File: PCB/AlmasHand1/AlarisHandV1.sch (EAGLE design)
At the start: 13 parts, among them M1 22-23-2021, M2 22-23-2021, M3 22-23-2021, M4 22-23-2021, M5 22-23-2021, M6 22-23-2021

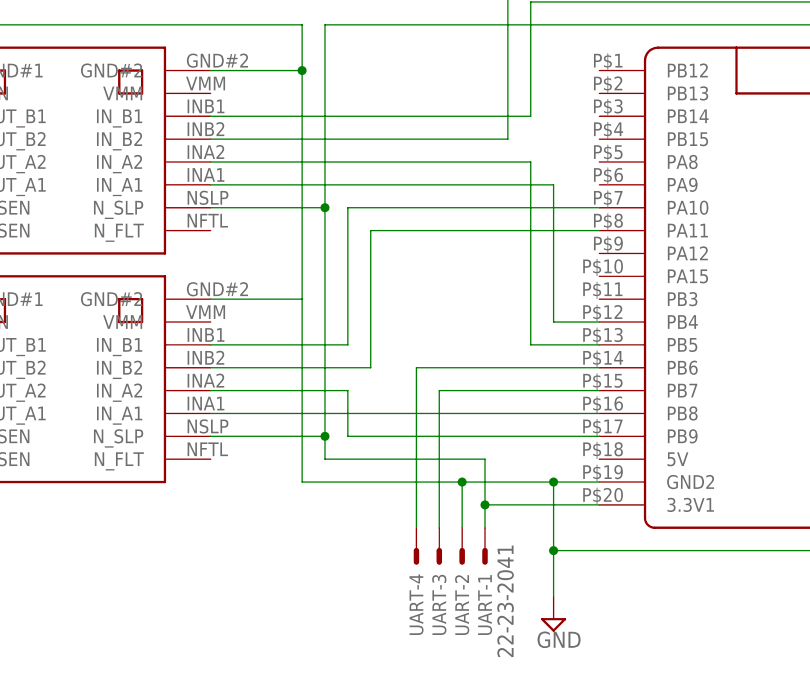
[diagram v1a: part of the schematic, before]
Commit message: fixed M1 port connection
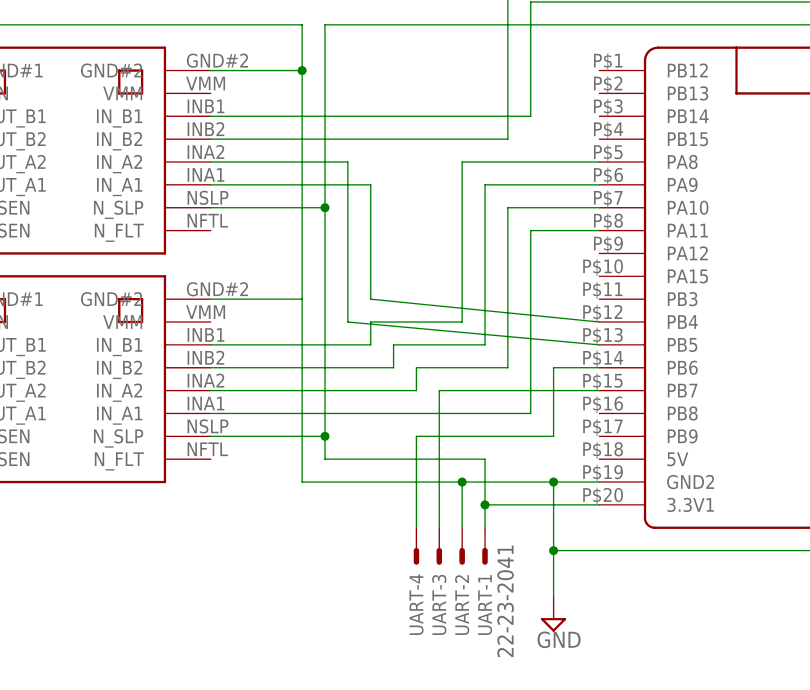
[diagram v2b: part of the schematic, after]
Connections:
- net UART_TX renamed N$1
- removed net N$1 (its old number): U$1.IN_A1, U$4.PB8
- new net N$9: U$1.IN_B1, U$4.PA8
- net N$2: now also U$1.IN_A1, U$4.PA11; no longer U$1.IN_A2, U$4.PB9
- net N$3: now also U$1.IN_A2; no longer U$1.IN_B1
- net N$4: now also U$4.PA9; no longer U$4.PA11
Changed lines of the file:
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@@
-</segment>
-</net>
-<net name="N$1" class="0">
-<segment>
-<pinref part="U$4" gate="G$1" pin="PB8"/>
-<pinref part="U$1" gate="G$1" pin="IN_A1"/>
-<wire x1="78.74" y1="66.04" x2="35.56" y2="66.04" width="0.1524" layer="91"/>
-</segment>
-</net>
-<net name="N$2" class="0">
-<segment>
-<pinref part="U$4" gate="G$1" pin="PB9"/>
-<wire x1="78.74" y1="63.5" x2="50.8" y2="63.5" width="0.1524" layer="91"/>
-<wire x1="50.8" y1="63.5" x2="50.8" y2="68.58" width="0.1524" layer="91"/>
-<pinref part="U$1" gate="G$1" pin="IN_A2"/>
-<wire x1="50.8" y1="68.58" x2="35.56" y2="68.58" width="0.1524" layer="91"/>
-</segment>
-</net>
-<net name="N$3" class="0">
-<segment>
-<pinref part="U$4" gate="G$1" pin="PA10"/>
-<wire x1="78.74" y1="88.9" x2="50.8" y2="88.9" width="0.1524" layer="91"/>
-<wire x1="50.8" y1="88.9" x2="50.8" y2="73.66" width="0.1524" layer="91"/>
-<pinref part="U$1" gate="G$1" pin="IN_B1"/>
-<wire x1="50.8" y1="73.66" x2="35.56" y2="73.66" width="0.1524" layer="91"/>
-</segment>
-</net>
-<net name="N$4" class="0">
-<segment>
-<pinref part="U$4" gate="G$1" pin="PA11"/>
-<wire x1="78.74" y1="86.36" x2="53.34" y2="86.36" width="0.1524" layer="91"/>
-<wire x1="53.34" y1="86.36" x2="53.34" y2="71.12" width="0.1524" layer="91"/>
-<pinref part="U$1" gate="G$1" pin="IN_B2"/>
-<wire x1="53.34" y1="71.12" x2="35.56" y2="71.12" width="0.1524" layer="91"/>
 </segment>
 </net>
@@
 <segment>
 <pinref part="U$4" gate="G$1" pin="PB4"/>
-<wire x1="78.74" y1="76.2" x2="73.66" y2="76.2" width="0.1524" layer="91"/>
-<wire x1="73.66" y1="76.2" x2="73.66" y2="91.44" width="0.1524" layer="91"/>
+<wire x1="78.74" y1="76.2" x2="53.34" y2="78.74" width="0.1524" layer="91"/>
+<wire x1="53.34" y1="78.74" x2="53.34" y2="91.44" width="0.1524" layer="91"/>
 <pinref part="U$2" gate="G$1" pin="IN_A1"/>
-<wire x1="73.66" y1="91.44" x2="35.56" y2="91.44" width="0.1524" layer="91"/>
+<wire x1="53.34" y1="91.44" x2="35.56" y2="91.44" width="0.1524" layer="91"/>
 </segment>
 </net>
@@
 <segment>
 <pinref part="U$4" gate="G$1" pin="PB5"/>
-<wire x1="78.74" y1="73.66" x2="71.12" y2="73.66" width="0.1524" layer="91"/>
-<wire x1="71.12" y1="73.66" x2="71.12" y2="93.98" width="0.1524" layer="91"/>
+<wire x1="78.74" y1="73.66" x2="50.8" y2="76.2" width="0.1524" layer="91"/>
+<wire x1="50.8" y1="76.2" x2="50.8" y2="93.98" width="0.1524" layer="91"/>
 <pinref part="U$2" gate="G$1" pin="IN_A2"/>
-<wire x1="71.12" y1="93.98" x2="35.56" y2="93.98" width="0.1524" layer="91"/>
+<wire x1="50.8" y1="93.98" x2="35.56" y2="93.98" width="0.1524" layer="91"/>
 </segment>
 </net>
@@
 </segment>
 </net>
-<net name="UART_TX" class="0">
+<net name="N$1" class="0">
 <segment>
 <pinref part="UART" gate="-4" pin="S"/>
+<wire x1="58.42" y1="53.34" x2="58.42" y2="63.5" width="0.1524" layer="91"/>
+<wire x1="58.42" y1="63.5" x2="73.66" y2="63.5" width="0.1524" layer="91"/>
 <pinref part="U$4" gate="G$1" pin="PB6"/>
-<wire x1="58.42" y1="53.34" x2="58.42" y2="71.12" width="0.1524" layer="91"/>
-<wire x1="58.42" y1="71.12" x2="78.74" y2="71.12" width="0.1524" layer="91"/>
-</segment>
-</net>
+<wire x1="73.66" y1="63.5" x2="73.66" y2="71.12" width="0.1524" layer="91"/>
+<wire x1="73.66" y1="71.12" x2="78.74" y2="71.12" width="0.1524" layer="91"/>
+</segment>
+</net>
+<net name="N$2" class="0">
+<segment>
+<pinref part="U$1" gate="G$1" pin="IN_A1"/>
+<wire x1="35.56" y1="66.04" x2="71.12" y2="66.04" width="0.1524" layer="91"/>
+<wire x1="71.12" y1="66.04" x2="71.12" y2="86.36" width="0.1524" layer="91"/>
+<pinref part="U$4" gate="G$1" pin="PA11"/>
+<wire x1="71.12" y1="86.36" x2="78.74" y2="86.36" width="0.1524" layer="91"/>
+</segment>
+</net>
+<net name="N$3" class="0">
+<segment>
+<pinref part="U$4" gate="G$1" pin="PA10"/>
+<wire x1="78.74" y1="88.9" x2="68.58" y2="88.9" width="0.1524" layer="91"/>
+<wire x1="68.58" y1="88.9" x2="68.58" y2="71.12" width="0.1524" layer="91"/>
+<wire x1="68.58" y1="71.12" x2="58.42" y2="71.12" width="0.1524" layer="91"/>
+<wire x1="58.42" y1="71.12" x2="58.42" y2="68.58" width="0.1524" layer="91"/>
+<pinref part="U$1" gate="G$1" pin="IN_A2"/>
+<wire x1="58.42" y1="68.58" x2="35.56" y2="68.58" width="0.1524" layer="91"/>
+</segment>
+</net>
+<net name="N$4" class="0">
+<segment>
+<pinref part="U$1" gate="G$1" pin="IN_B2"/>
+<wire x1="35.56" y1="71.12" x2="55.88" y2="71.12" width="0.1524" layer="91"/>
+<wire x1="55.88" y1="71.12" x2="55.88" y2="73.66" width="0.1524" layer="91"/>
+<wire x1="55.88" y1="73.66" x2="66.04" y2="73.66" width="0.1524" layer="91"/>
+<wire x1="66.04" y1="73.66" x2="66.04" y2="91.44" width="0.1524" layer="91"/>
+<pinref part="U$4" gate="G$1" pin="PA9"/>
+<wire x1="66.04" y1="91.44" x2="78.74" y2="91.44" width="0.1524" layer="91"/>
+</segment>
+</net>
+<net name="N$9" class="0">
+<segment>
+<pinref part="U$4" gate="G$1" pin="PA8"/>
+<wire x1="78.74" y1="93.98" x2="63.5" y2="93.98" width="0.1524" layer="91"/>
+<wire x1="63.5" y1="93.98" x2="63.5" y2="76.2" width="0.1524" layer="91"/>
+<wire x1="63.5" y1="76.2" x2="53.34" y2="76.2" width="0.1524" layer="91"/>
+<wire x1="53.34" y1="76.2" x2="53.34" y2="73.66" width="0.1524" layer="91"/>
+<pinref part="U$1" gate="G$1" pin="IN_B1"/>
+<wire x1="53.34" y1="73.66" x2="35.56" y2="73.66" width="0.1524" layer="91"/>
+</segment>
+</net>
